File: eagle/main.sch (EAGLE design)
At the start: 13 parts, among them IC1 7805TV, U1 INA213AIDCKT, U2 LM1117MP-3.3

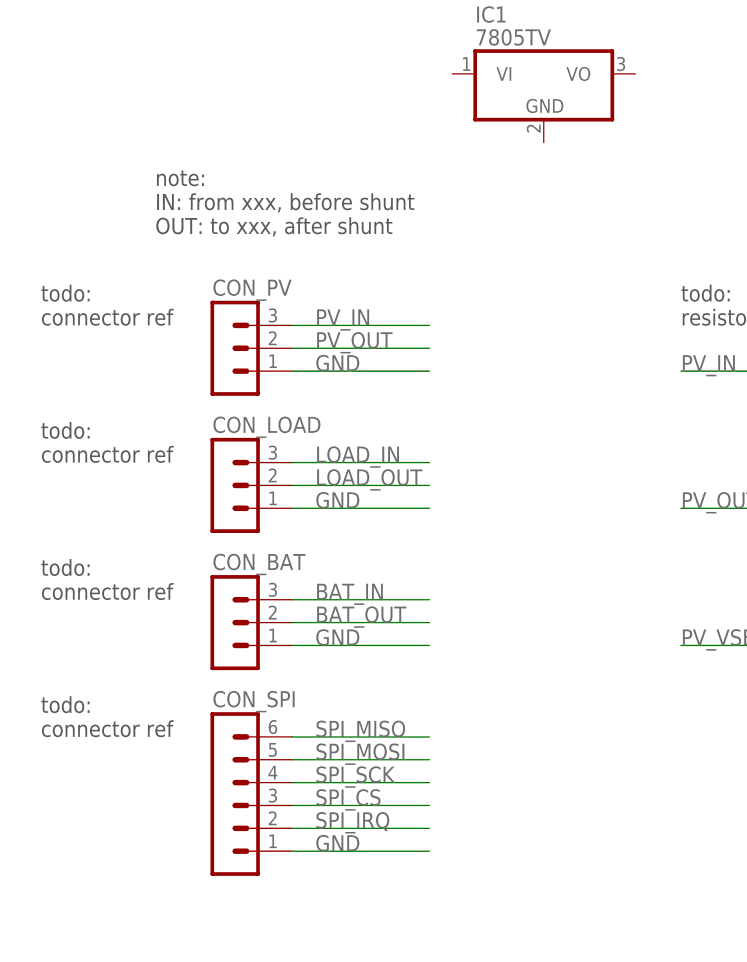
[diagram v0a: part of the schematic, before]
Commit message: add eagle/main.brd, eagle/lib/misc
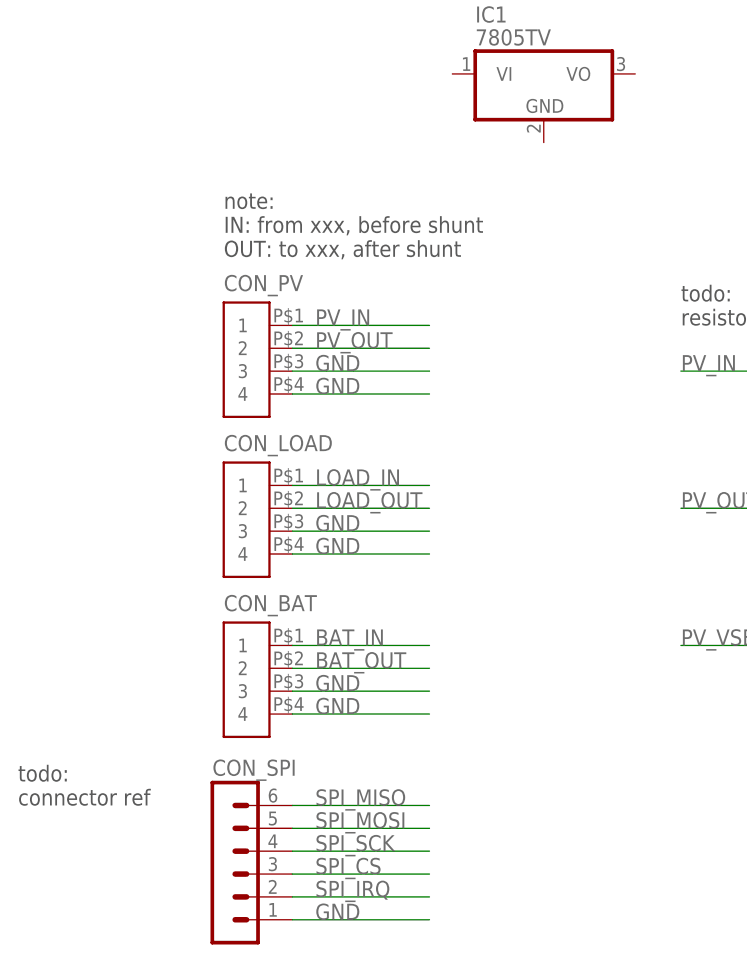
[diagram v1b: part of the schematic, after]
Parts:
- CON_BAT, CON_LOAD, CON_PV: value (none) -> MC000036; device con-lstb:MA03-1 -> MC000036:MC000036
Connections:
- net BAT_IN: now also CON_BAT.1; no longer CON_BAT.3
- net GND: now also CON_BAT.3, CON_BAT.4, CON_LOAD.3, CON_LOAD.4, CON_PV.3, CON_PV.4; no longer CON_BAT.1, CON_LOAD.1, CON_PV.1
- net LOAD_IN: now also CON_LOAD.1; no longer CON_LOAD.3
- net PV_IN: now also CON_PV.1; no longer CON_PV.3
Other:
- moved on the sheet: CON_SPI
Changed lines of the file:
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@@
 <part name="U2" library="NSC-LM1117MP-3.3" deviceset="LM1117MP-3.3" device=""/>
 <part name="CON_SPI" library="con-lstb" deviceset="MA06-1" device=""/>
-<part name="CON_PV" library="con-lstb" deviceset="MA03-1" device=""/>
-<part name="CON_LOAD" library="con-lstb" deviceset="MA03-1" device=""/>
-<part name="CON_BAT" library="con-lstb" deviceset="MA03-1" device=""/>
 <part name="GND1" library="supply1" deviceset="GND" device=""/>
 <part name="C1" library="rcl" deviceset="C-EU" device="C1206" value="100n"/>
 <part name="C2" library="rcl" deviceset="C-EU" device="C1206" value="100n"/>
 <part name="GND2" library="supply1" deviceset="GND" device=""/>
+<part name="CON_PV" library="MC000036" deviceset="MC000036" device=""/>
+<part name="CON_LOAD" library="MC000036" deviceset="MC000036" device=""/>
+<part name="CON_BAT" library="MC000036" deviceset="MC000036" device=""/>
 </parts>
 <sheets>
@@
 <text x="20.32" y="246.38" size="1.778" layer="97">todo:
 jumper to select USB or 5V</text>
-<text x="-12.7" y="208.28" size="1.778" layer="97">note:
+<text x="-5.08" y="205.74" size="1.778" layer="97">note:
 IN: from xxx, before shunt
 OUT: to xxx, after shunt</text>
 <text x="111.76" y="149.86" size="1.778" layer="97">todo:
 bypass cap ref</text>
-<text x="-25.4" y="152.4" size="1.778" layer="97">todo:
-connector ref</text>
-<text x="-25.4" y="167.64" size="1.778" layer="97">todo:
-connector ref</text>
-<text x="-25.4" y="182.88" size="1.778" layer="97">todo:
-connector ref</text>
-<text x="-25.4" y="198.12" size="1.778" layer="97">todo:
+<text x="-27.94" y="144.78" size="1.778" layer="97">todo:
 connector ref</text>
 </plain>
@@
 <instance part="U$1" gate="G$1" x="210.82" y="195.58"/>
 <instance part="U2" gate="A" x="88.9" y="223.52"/>
-<instance part="CON_SPI" gate="1" x="-5.08" y="147.32"/>
-<instance part="CON_PV" gate="G$1" x="-5.08" y="195.58"/>
-<instance part="CON_LOAD" gate="G$1" x="-5.08" y="180.34"/>
-<instance part="CON_BAT" gate="G$1" x="-5.08" y="165.1"/>
+<instance part="CON_SPI" gate="1" x="-5.08" y="139.7"/>
 <instance part="GND1" gate="1" x="60.96" y="142.24"/>
 <instance part="C1" gate="G$1" x="68.58" y="154.94"/>
 <instance part="C2" gate="G$1" x="104.14" y="152.4"/>
 <instance part="GND2" gate="1" x="104.14" y="142.24"/>
+<instance part="CON_PV" gate="G$1" x="-2.54" y="193.04"/>
+<instance part="CON_LOAD" gate="G$1" x="-2.54" y="175.26"/>
+<instance part="CON_BAT" gate="G$1" x="-2.54" y="157.48"/>
 </instances>
 <busses>
@@
 <segment>
 <pinref part="CON_SPI" gate="1" pin="6"/>
-<wire x1="2.54" y1="152.4" x2="17.78" y2="152.4" width="0.1524" layer="91"/>
-<label x="5.08" y="152.4" size="1.778" layer="95"/>
-</segment>
-</net>
-<net name="SPI_MOSI" class="0">
-<segment>
-<pinref part="CON_SPI" gate="1" pin="5"/>
-<wire x1="2.54" y1="149.86" x2="17.78" y2="149.86" width="0.1524" layer="91"/>
-<label x="5.08" y="149.86" size="1.778" layer="95"/>
-</segment>
-</net>
-<net name="SPI_SCK" class="0">
-<segment>
-<pinref part="CON_SPI" gate="1" pin="4"/>
-<wire x1="2.54" y1="147.32" x2="17.78" y2="147.32" width="0.1524" layer="91"/>
-<label x="5.08" y="147.32" size="1.778" layer="95"/>
-</segment>
-</net>
-<net name="SPI_CS" class="0">
-<segment>
-<pinref part="CON_SPI" gate="1" pin="3"/>
 <wire x1="2.54" y1="144.78" x2="17.78" y2="144.78" width="0.1524" layer="91"/>
 <label x="5.08" y="144.78" size="1.778" layer="95"/>
 </segment>
 </net>
-<net name="SPI_IRQ" class="0">
-<segment>
-<pinref part="CON_SPI" gate="1" pin="2"/>
+<net name="SPI_MOSI" class="0">
+<segment>
+<pinref part="CON_SPI" gate="1" pin="5"/>
 <wire x1="2.54" y1="142.24" x2="17.78" y2="142.24" width="0.1524" layer="91"/>
 <label x="5.08" y="142.24" size="1.778" layer="95"/>
 </segment>
 </net>
-<net name="GND" class="0">
-<segment>
-<pinref part="CON_SPI" gate="1" pin="1"/>
+<net name="SPI_SCK" class="0">
+<segment>
+<pinref part="CON_SPI" gate="1" pin="4"/>
 <wire x1="2.54" y1="139.7" x2="17.78" y2="139.7" width="0.1524" layer="91"/>
 <label x="5.08" y="139.7" size="1.778" layer="95"/>
 </segment>
-<segment>
-<pinref part="CON_PV" gate="G$1" pin="1"/>
+</net>
+<net name="SPI_CS" class="0">
+<segment>
+<pinref part="CON_SPI" gate="1" pin="3"/>
+<wire x1="2.54" y1="137.16" x2="17.78" y2="137.16" width="0.1524" layer="91"/>
+<label x="5.08" y="137.16" size="1.778" layer="95"/>
+</segment>
+</net>
+<net name="SPI_IRQ" class="0">
+<segment>
+<pinref part="CON_SPI" gate="1" pin="2"/>
+<wire x1="2.54" y1="134.62" x2="17.78" y2="134.62" width="0.1524" layer="91"/>
+<label x="5.08" y="134.62" size="1.778" layer="95"/>
+</segment>
+</net>
+<net name="GND" class="0">
+<segment>
+<pinref part="CON_SPI" gate="1" pin="1"/>
+<wire x1="2.54" y1="132.08" x2="17.78" y2="132.08" width="0.1524" layer="91"/>
+<label x="5.08" y="132.08" size="1.778" layer="95"/>
+</segment>
+<segment>
 <wire x1="2.54" y1="193.04" x2="17.78" y2="193.04" width="0.1524" layer="91"/>
 <label x="5.08" y="193.04" size="1.778" layer="95"/>
-</segment>
-<segment>
-<pinref part="CON_LOAD" gate="G$1" pin="1"/>
-<wire x1="2.54" y1="177.8" x2="17.78" y2="177.8" width="0.1524" layer="91"/>
-<label x="5.08" y="177.8" size="1.778" layer="95"/>
-</segment>
-<segment>
-<pinref part="CON_BAT" gate="G$1" pin="1"/>
-<wire x1="2.54" y1="162.56" x2="17.78" y2="162.56" width="0.1524" layer="91"/>
-<label x="5.08" y="162.56" size="1.778" layer="95"/>
+<pinref part="CON_PV" gate="G$1" pin="3"/>
+</segment>
+<segment>
+<wire x1="2.54" y1="175.26" x2="17.78" y2="175.26" width="0.1524" layer="91"/>
+<label x="5.08" y="175.26" size="1.778" layer="95"/>
+<pinref part="CON_LOAD" gate="G$1" pin="3"/>
+</segment>
+<segment>
+<wire x1="2.54" y1="157.48" x2="17.78" y2="157.48" width="0.1524" layer="91"/>
+<label x="5.08" y="157.48" size="1.778" layer="95"/>
+<pinref part="CON_BAT" gate="G$1" pin="3"/>
 </segment>
 <segment>
@@
 <pinref part="GND2" gate="1" pin="GND"/>
 </segment>
+<segment>
+<wire x1="2.54" y1="190.5" x2="17.78" y2="190.5" width="0.1524" layer="91"/>
+<label x="5.08" y="190.5" size="1.778" layer="95"/>
+<pinref part="CON_PV" gate="G$1" pin="4"/>
+</segment>
+<segment>
+<wire x1="2.54" y1="172.72" x2="17.78" y2="172.72" width="0.1524" layer="91"/>
+<label x="5.08" y="172.72" size="1.778" layer="95"/>
+<pinref part="CON_LOAD" gate="G$1" pin="4"/>
+</segment>
+<segment>
+<wire x1="2.54" y1="154.94" x2="17.78" y2="154.94" width="0.1524" layer="91"/>
+<label x="5.08" y="154.94" size="1.778" layer="95"/>
+<pinref part="CON_BAT" gate="G$1" pin="4"/>
+</segment>
 </net>
 <net name="PV_IN" class="0">
 <segment>
-<pinref part="CON_PV" gate="G$1" pin="3"/>
 <wire x1="2.54" y1="198.12" x2="17.78" y2="198.12" width="0.1524" layer="91"/>
 <label x="5.08" y="198.12" size="1.778" layer="95"/>
+<pinref part="CON_PV" gate="G$1" pin="1"/>
 </segment>
 <segment>
@@
 <net name="PV_OUT" class="0">
 <segment>
-<pinref part="CON_PV" gate="G$1" pin="2"/>
 <wire x1="2.54" y1="195.58" x2="17.78" y2="195.58" width="0.1524" layer="91"/>
 <label x="5.08" y="195.58" size="1.778" layer="95"/>
+<pinref part="CON_PV" gate="G$1" pin="2"/>
 </segment>
 <segment>
@@
 <net name="LOAD_IN" class="0">
 <segment>
-<pinref part="CON_LOAD" gate="G$1" pin="3"/>
-<wire x1="2.54" y1="182.88" x2="17.78" y2="182.88" width="0.1524" layer="91"/>
-<label x="5.08" y="182.88" size="1.778" layer="95"/>
-</segment>
-</net>
-<net name="LOAD_OUT" class="0">
-<segment>
-<pinref part="CON_LOAD" gate="G$1" pin="2"/>
 <wire x1="2.54" y1="180.34" x2="17.78" y2="180.34" width="0.1524" layer="91"/>
 <label x="5.08" y="180.34" size="1.778" layer="95"/>
+<pinref part="CON_LOAD" gate="G$1" pin="1"/>
+</segment>
+</net>
+<net name="LOAD_OUT" class="0">
+<segment>
+<wire x1="2.54" y1="177.8" x2="17.78" y2="177.8" width="0.1524" layer="91"/>
+<label x="5.08" y="177.8" size="1.778" layer="95"/>
+<pinref part="CON_LOAD" gate="G$1" pin="2"/>
 </segment>
 </net>
 <net name="BAT_IN" class="0">
 <segment>
-<pinref part="CON_BAT" gate="G$1" pin="3"/>
-<wire x1="2.54" y1="167.64" x2="17.78" y2="167.64" width="0.1524" layer="91"/>
-<label x="5.08" y="167.64" size="1.778" layer="95"/>
+<wire x1="2.54" y1="162.56" x2="17.78" y2="162.56" width="0.1524" layer="91"/>
+<label x="5.08" y="162.56" size="1.778" layer="95"/>
+<pinref part="CON_BAT" gate="G$1" pin="1"/>
 </segment>
 </net>
 <net name="BAT_OUT" class="0">
 <segment>
+<wire x1="2.54" y1="160.02" x2="17.78" y2="160.02" width="0.1524" layer="91"/>
+<label x="5.08" y="160.02" size="1.778" layer="95"/>
 <pinref part="CON_BAT" gate="G$1" pin="2"/>
-<wire x1="2.54" y1="165.1" x2="17.78" y2="165.1" width="0.1524" layer="91"/>
-<label x="5.08" y="165.1" size="1.778" layer="95"/>
-</segment>
-</net>
+</segment>
+</net>

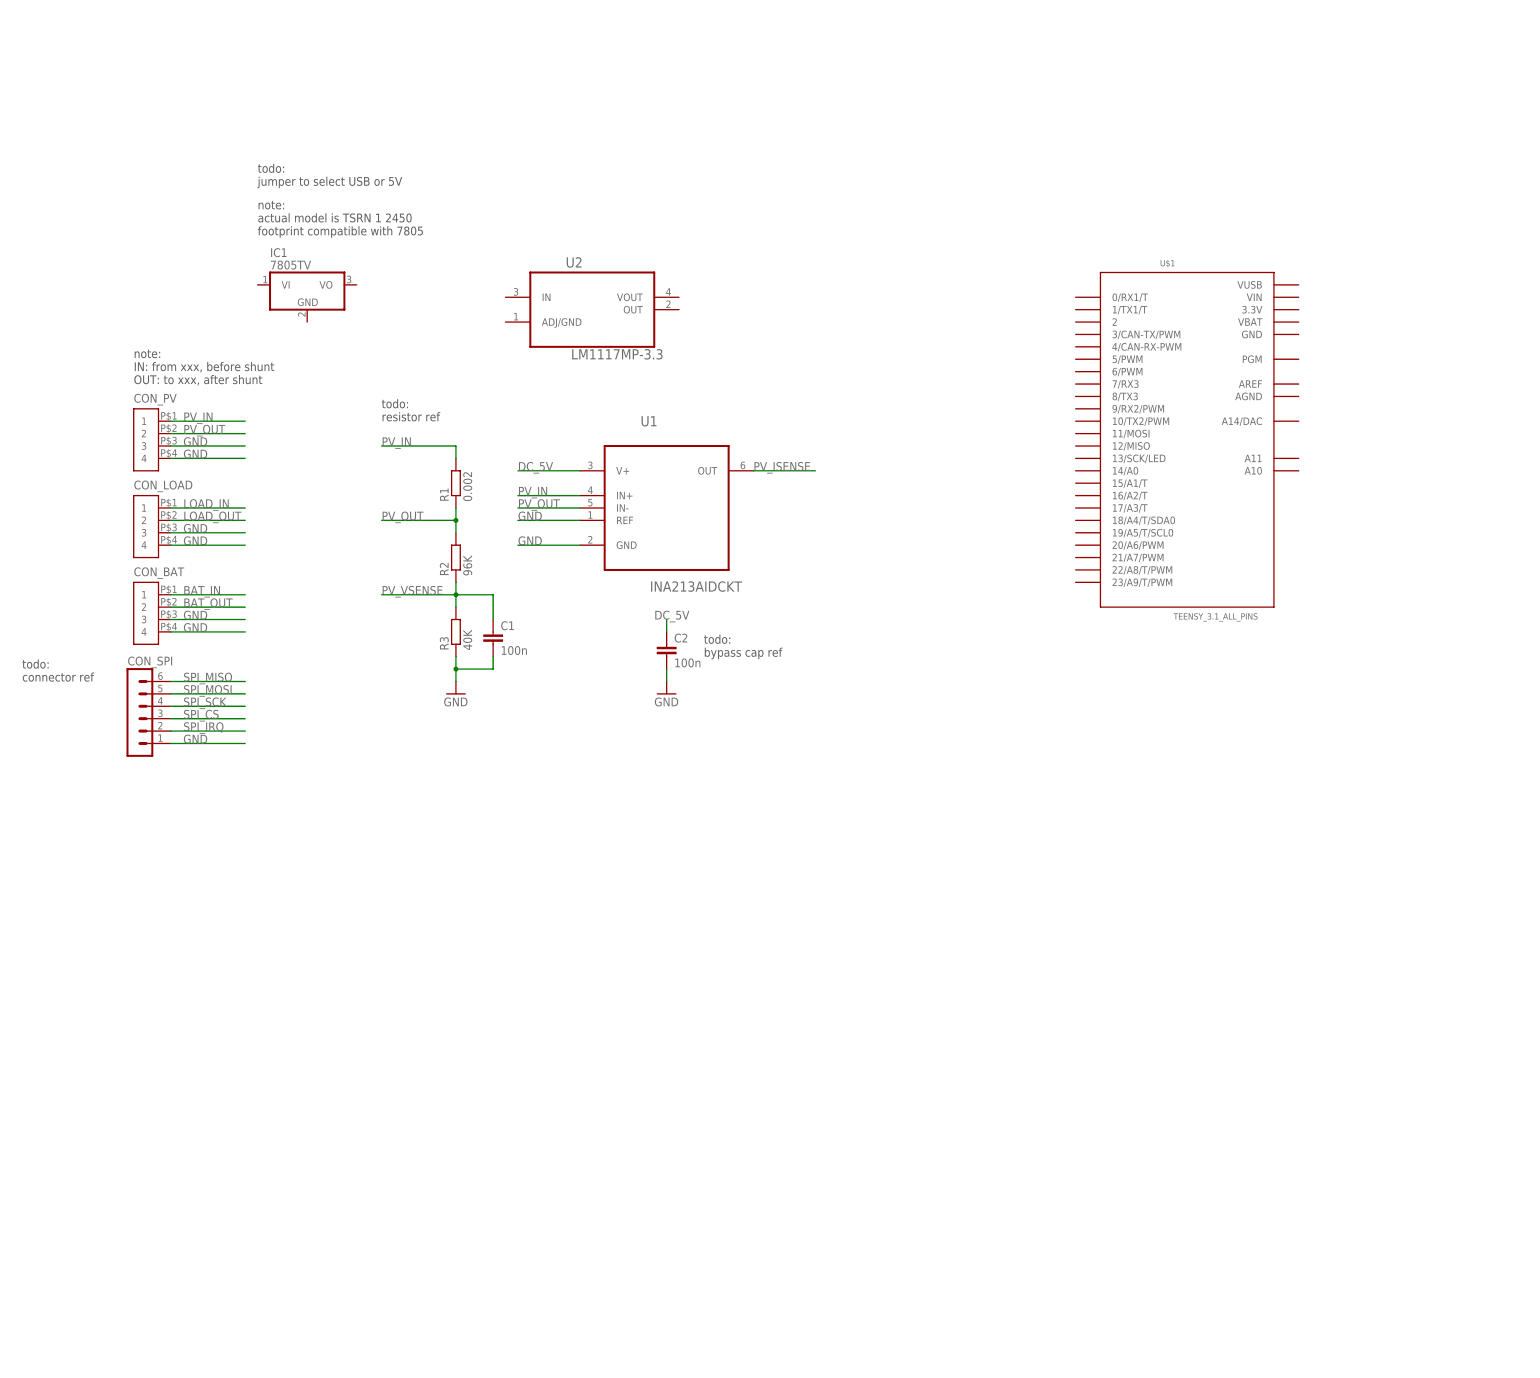
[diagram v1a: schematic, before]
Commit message: add microsd
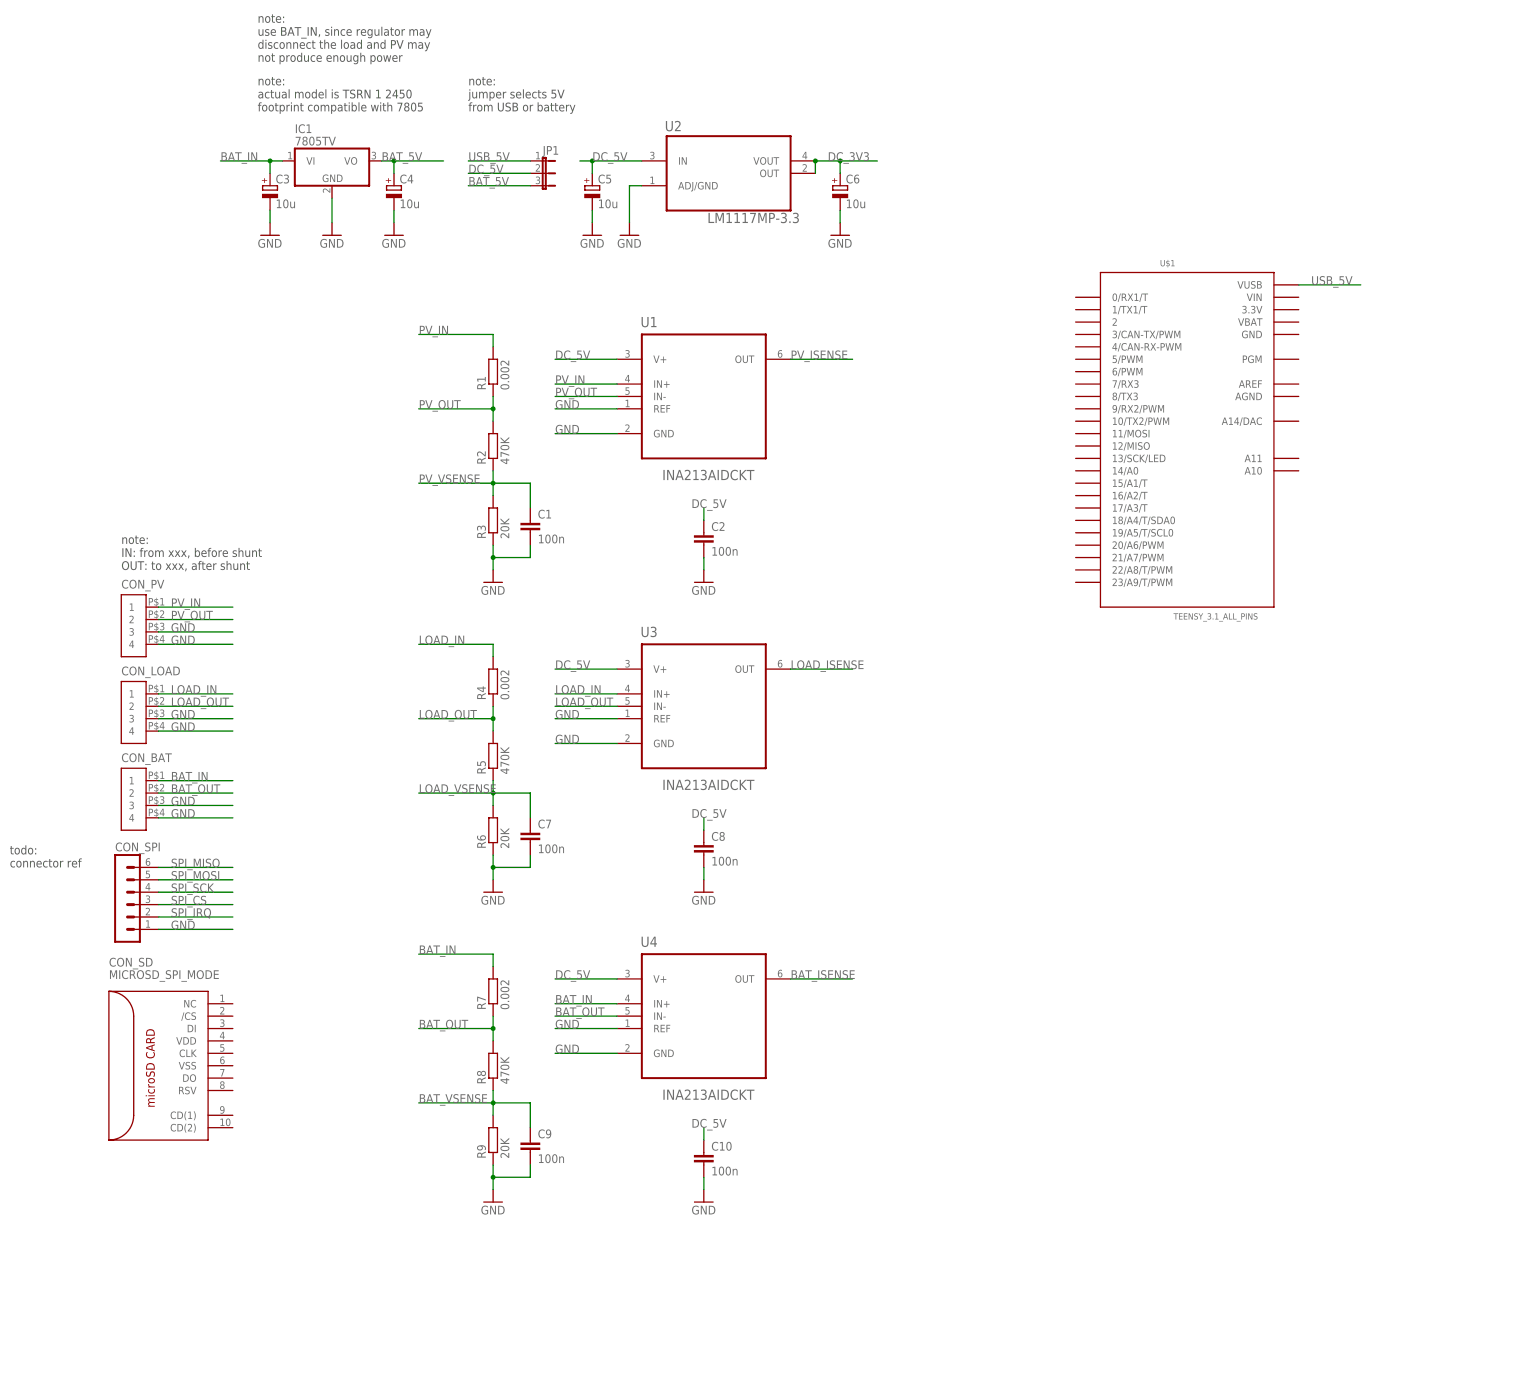
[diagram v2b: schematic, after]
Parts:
- added C10, C7, C8, C9: 100n, rcl:C-EUC1206
- added C3, C4, C5, C6: 10u, rcl:CPOL-EUCT3528
- added CON_SD: MICROSD_SPI_MODE, con-molex-microsd:MICROSD_SPI_MODE
- added JP1: (no value), jumper:JP2E
- added R4, R7: 0.002, resistor:R-EU_R2512
- added R5, R8: 470K, rcl:R-EU_R0603
- added R6, R9: 20K, rcl:R-EU_R0603
- added U3, U4: INA213AIDCKT, TI-INA213AIDCKT:INA213AIDCKT
- R2: value 96K -> 470K; device resistor:R-EU_R2512 -> rcl:R-EU_R0603
- R3: value 40K -> 20K; device resistor:R-EU_R2512 -> rcl:R-EU_R0603
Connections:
- new net BAT_5V: C4.+, IC1.VO, JP1.3
- new net BAT_ISENSE: U4.OUT
- new net BAT_VSENSE: C9.1, R8.1, R9.2
- new net DC_3V3: C6.+, U2.OUT, U2.VOUT
- new net LOAD_ISENSE: U3.OUT
- new net LOAD_VSENSE: C7.1, R5.1, R6.2
- new net USB_5V: JP1.1, U$1.VUSB
- net BAT_IN: now also C3.+, IC1.VI, R7.2, U4.IN+
- net BAT_OUT: now also R7.1, R8.2, U4.IN-
- net DC_5V: now also C10.1, C5.+, C8.1, JP1.2, U2.IN, U3.V+, U4.V+
- net GND: now also C10.2, C3.-, C4.-, C5.-, C6.-, C7.2, C8.2, C9.2, IC1.GND, R6.1, R9.1, U2.ADJ/GND, U3.GND, U3.REF, U4.GND, U4.REF
- net LOAD_IN: now also R4.2, U3.IN+
- net LOAD_OUT: now also R4.1, R5.2, U3.IN-
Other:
- note added: "note: jumper selects 5V from USB or battery"
- note added: "note: use BAT_IN, since regulator may disconnect the load and PV may not produce enough power"
- note removed: "todo: bypass cap ref"
- note removed: "todo: jumper to select USB or 5V"
- note removed: "todo: resistor ref"
- moved on the sheet: C1, C2, CON_BAT, CON_LOAD, CON_PV, CON_SPI, IC1, R1, R2, R3, U1, U2
